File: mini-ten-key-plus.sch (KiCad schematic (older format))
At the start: 65 parts, among them SW0 SW_Push, U0 ProMicro

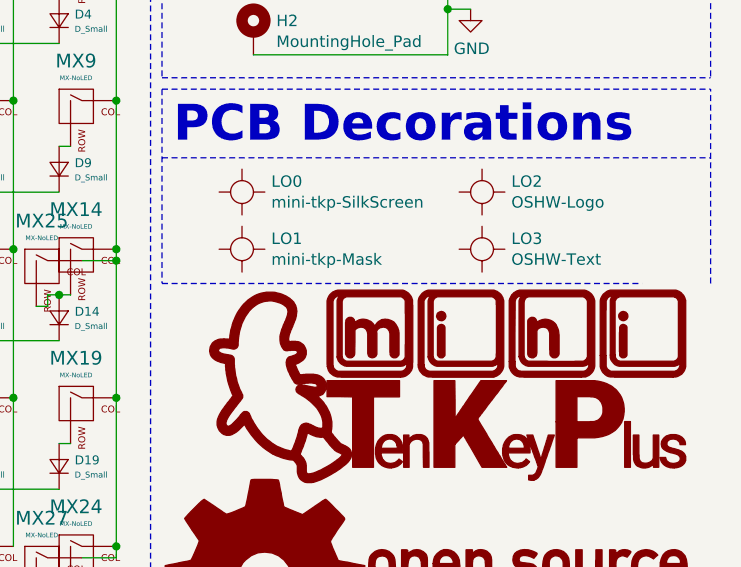
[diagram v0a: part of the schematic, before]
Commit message: Added additional info to PCB/Schematic and added PCB/Schematic PDF
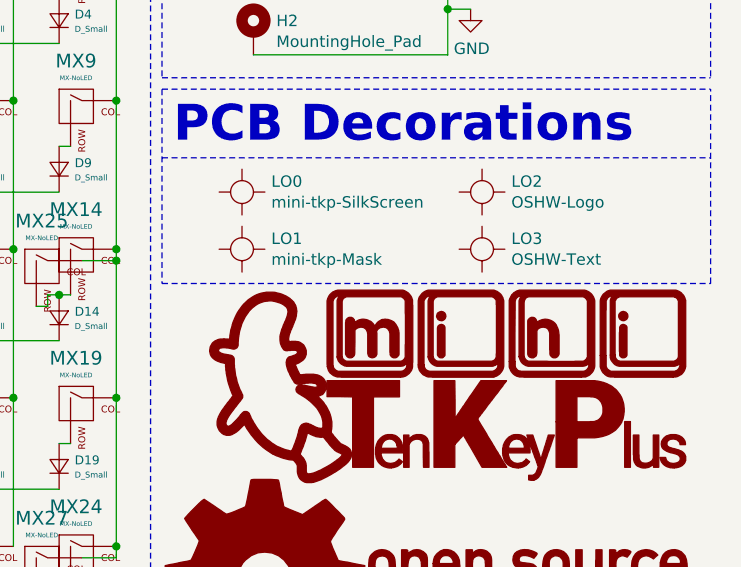
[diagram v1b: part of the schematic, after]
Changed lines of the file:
@@
 encoding utf-8
 Sheet 1 1
-Title ""
-Date ""
-Rev ""
-Comp ""
-Comment1 ""
-Comment2 ""
-Comment3 ""
-Comment4 ""
+Title "Ten Key Plus"
+Date "2021-12-21"
+Rev "1.a"
+Comp "Full License: https://github.com/minibois/ten-key-plus/tree/master/LICENSE"
+Comment1 "of CERN_OHL-S v2 (https://ohwr.org/cern_ohl_s_v2.txt)"
+Comment2 "You may redistribute and modify this source and make products using it under the terms"
+Comment3 "This schematic describes Open Hardware and is licensed under the CERN-OHL-S v2."
+Comment4 "Copyright minibois 2021. "
 $EndDescr
 $Comp
@@
 	3200 500  3200 1650
 Wire Notes Line
-	3200 4800 5300 4800
-Wire Notes Line
 	3200 3950 3200 4800
 Wire Notes Line
@@
 Wire Notes Line
 	3200 4250 5600 4250
+Wire Notes Line
+	3200 4800 5600 4800
 $EndSCHEMATC
